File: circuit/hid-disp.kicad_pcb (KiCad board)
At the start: 2 copper layers, 43 x 25 mm, 18 parts, among them J1 USB, J2 PROG, U1 ATtiny85-20S, U2 AMS1117-3.3, U3 TXB0102DCU, U4 74ACT164, U5 HDSP-A153

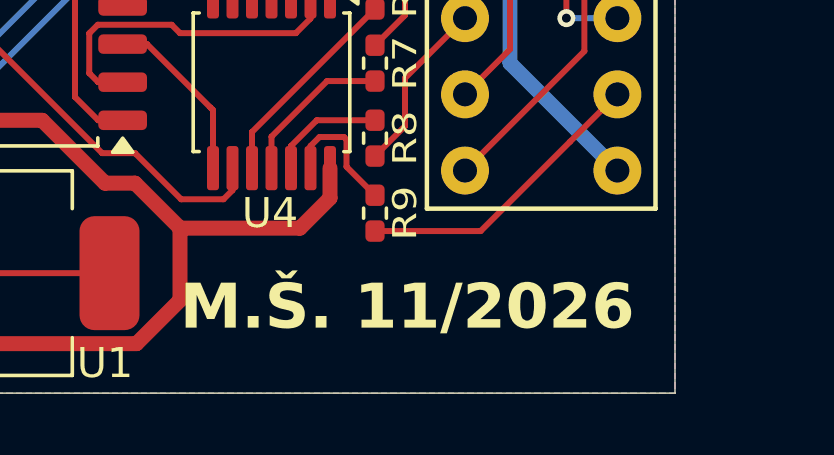
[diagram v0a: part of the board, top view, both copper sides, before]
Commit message: URL printed on pcb
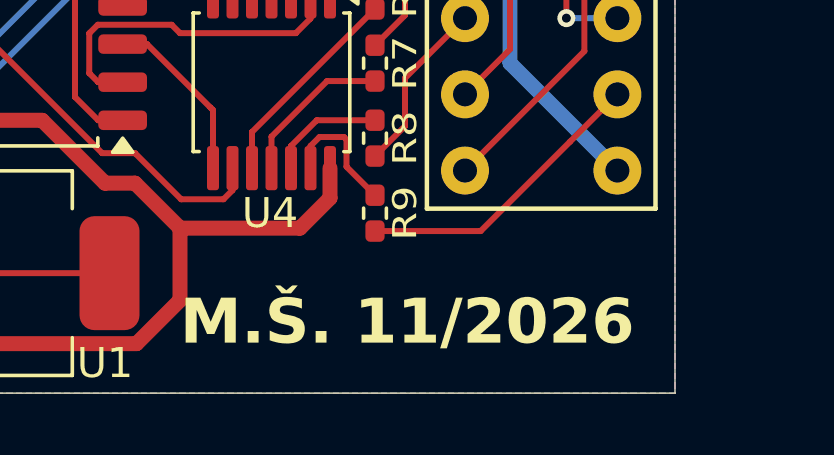
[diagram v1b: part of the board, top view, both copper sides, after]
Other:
- board text added: "http://github.com/milan-simanek/hid-disp"
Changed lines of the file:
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@@
 		)
 		(property "Value" "AMS1117-3.3"
-			(at 0 4.5 0)
+			(at 0.5 4.5 0)
 			(layer "F.Fab")
 			(effects
@@
 	)
 	(gr_line
-		(start 117 121)
-		(end 159 121)
+		(start 114.5 121)
+		(end 157.5 121)
 		(stroke
 			(width 0.1)
@@
 	)
 	(gr_text "M.Š. 11/2026"
-		(at 141 131.5 0)
+		(at 141 132 0)
 		(layer "F.SilkS")
 		(effects
@@
 		)
 	)
+	(gr_text "http://github.com/milan-simanek/hid-disp"
+		(at 157.5 132.5 0)
+		(layer "B.SilkS")
+		(effects
+			(font
+				(size 1 0.9)
+				(thickness 0.2)
+				(bold yes)
+			)
+			(justify left bottom mirror)
+		)
+	)
